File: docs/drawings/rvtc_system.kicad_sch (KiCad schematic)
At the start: 0 parts

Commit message: Diagram: add MeshCore nodes, bridge ports, other LAN hosts
From MikroTik DHCP leases: MeshCore Observer (.25, ESP32-S3, WiFi,
MQTT direct to Mosquitto) and companion (.26, RAK4631+RAK13800,
ether4, TCP to Meshy); meshcore_name_resolver.py adaptor; ether6/ether4
labels on gateway and host links; box of other RV LAN hosts (no MACs).
Title block now marks the .kicad_sch as hand-editable base layout.

Co-Authored-By: Claude Opus 5.5 <noreply@anthropic.com>
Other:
- note added: ".2 VE7CBH-RV workstation (ether4) .4 DS223 NAS (ether5) .20 printer .21 Fanvil X4G phone .22 TL-SG108PE PoE switch (ether4) .23 Motorola phone .24 WP-820 (wlan1) .254 Sonoff S31 plug (dynamic, wlan1)"
- note added: "ADVERTs -> meshcore/names/+"
- note added: "Arrow = data direction. Gateway IPs are 192.168.88.x, port 4001."
- note added: "ESP32-S3, WiFi (wlan1) MQTT meshcore/DUQ/+/* -> :1883"
- note added: "Ethernet - TCP/IP"
- note added: "MeshCore Observer .25"
- note added: "MeshCore companion .26"
- note added: "Other RV LAN hosts"
- note added: "RAK4631 + RAK13800 (WIZnet), ether4 TCP <-> Meshy app"
- note added: "Source: RVTC_System_Reference_2_15.md"
- note added: "WiFi - TCP/IP"
- note added: "ether4"
- note added: "ether6"
- note added: "meshcore/DUQ/+/*: published by"
- note added: "meshcore_name_resolver.py"
- note added: "the nodes themselves (no bridge)"
- note removed: "Arrow = data direction. Gateway IPs are 192.168.88.x, port 4001. Source: RVTC_System_Reference_2_15.md"
- note removed: "Eth"

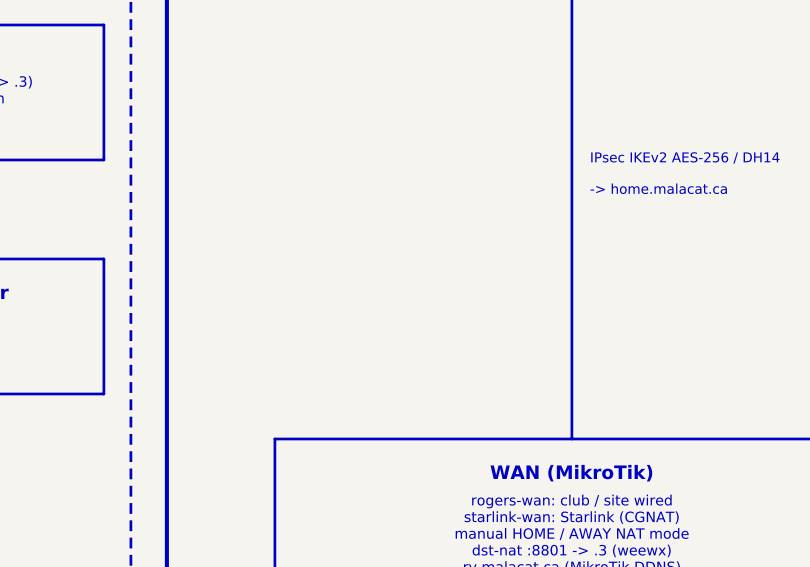
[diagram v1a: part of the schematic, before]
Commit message: Add electrical block diagram as page 2 of rvtc_system KiCad project
New rvtc_power.kicad_sch (+ generator): PV -> MPPT60 -> LiFePO4 bank
(main fuse, 300 A shunt, single-point ground) -> 12 V DC bus feeding the
OEM DC load centre, RVTC 12 V kit and the EVO-2212; shore/gen inlets with
KWS meters -> transfer -> EVO -> AC load centre, load-shed relays, A/C,
heater plugs, J45 monitors/speakers (the only AC-powered RVTC items).
Undocumented values marked "?" for hand completion.

rvtc_system.kicad_sch gets an "Electrical" sheet symbol linking page 2;
minimal rvtc_system.kicad_pro added so both open as one project.

Co-Authored-By: Claude Opus 5.5 <noreply@anthropic.com>
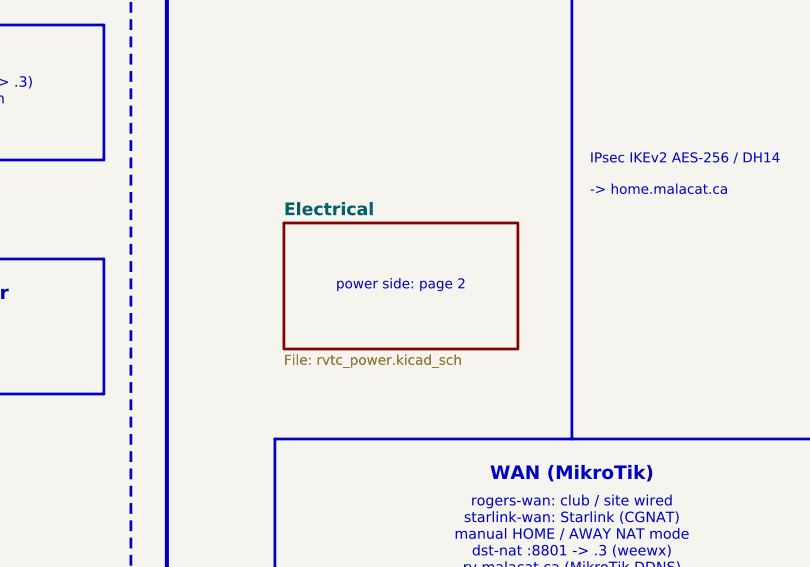
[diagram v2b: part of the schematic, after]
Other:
- added sheet Electrical (rvtc_power.kicad_sch)
- note added: "power side: page 2"
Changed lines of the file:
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@@
     (company "RVTC - VE7CBH")
     (comment 1 "Block-diagram style - not a manufacturable schematic")
-    (comment 2 "Base layout from docs/drawings/generate_rvtc_system_sch.py - hand-edited since; re-running it overwrites edits")
+    (comment 2 "Base layout: generate_rvtc_system_sch.py; hand-edited after - re-running overwrites")
   )
   (text "RV Total Control (RVTC) - System Block Diagram" (exclude_from_sim no) (at 12 14 0)
@@
     (effects (font (size 1.0 1.0)) (justify left))
   )
+  (sheet (at 343 172) (size 26 14) (fields_autoplaced yes)
+    (stroke (width 0.3) (type solid) (color 180 0 0 1))
+    (fill (color 253 230 230 1))
+    (property "Sheetname" "Electrical" (at 343 171.3 0)
+      (effects (font (size 1.4 1.4) bold) (justify left bottom))
+    )
+    (property "Sheetfile" "rvtc_power.kicad_sch" (at 343 186.6 0)
+      (effects (font (size 1.1 1.1)) (justify left top))
+    )
+    (instances
+      (project "rvtc_system"
+        (path "/7bcc9a8a-ae26-44fa-87de-cee0a644d8cb" (page "2"))
+      )
+    )
+  )
+  (text "power side: page 2" (exclude_from_sim no) (at 356 179 0)
+    (effects (font (size 1.1 1.1)))
+  )
   (sheet_instances

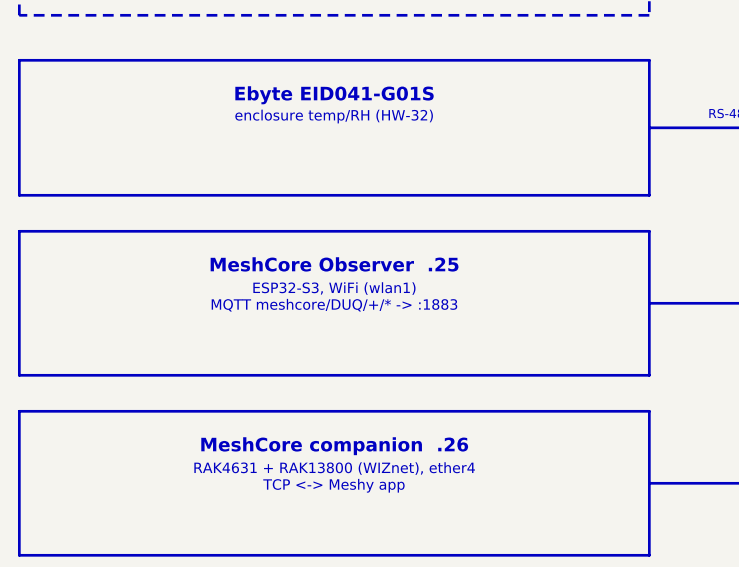
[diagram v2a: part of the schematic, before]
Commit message: Drawings: observer is a LilyGo T-Beam; fill in PV array from datasheet
Page 1: MeshCore Observer box now names VE7CBH-RVTC (LilyGo T-Beam,
DUQ, also reports to the public observer map) instead of "ESP32-S3".

Page 2 (includes the owner's hand edits so far, e.g. DC load centre
fuse 70 A and 3 string lines): PV array is 9 x Renogy RNG-100D-SS,
3S3P = 900 W; array Voc 72.9 V / Isc 15.6 A, Vmp 61.2 V / Imp 14.7 A
(from the panel datasheet). Combiner notes the 15 A panel max series
fuse rating.

Co-Authored-By: Claude Opus 5.5 <noreply@anthropic.com>
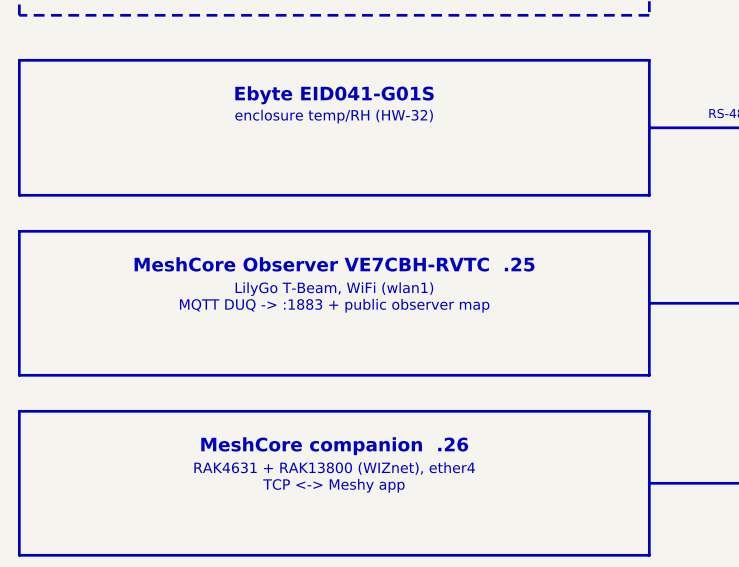
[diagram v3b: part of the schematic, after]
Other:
- note added: "LilyGo T-Beam, WiFi (wlan1) MQTT DUQ -> :1883 + public observer map"
- note added: "MeshCore Observer VE7CBH-RVTC .25"
- note removed: "ESP32-S3, WiFi (wlan1) MQTT meshcore/DUQ/+/* -> :1883"
- note removed: "MeshCore Observer .25"
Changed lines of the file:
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@@
     (fill (type color) (color 225 236 252 1))
   )
-  (text "MeshCore Observer  .25" (exclude_from_sim no) (at 47.0 253 0)
+  (text "MeshCore Observer VE7CBH-RVTC  .25" (exclude_from_sim no) (at 47.0 253 0)
     (effects (font (size 1.5 1.5) bold (color 0 70 160 1)))
   )
-  (text "ESP32-S3, WiFi (wlan1)\nMQTT meshcore/DUQ/+/* -> :1883" (exclude_from_sim no) (at 47.0 256.5 0)
+  (text "LilyGo T-Beam, WiFi (wlan1)\nMQTT DUQ -> :1883 + public observer map" (exclude_from_sim no) (at 47.0 256.5 0)
     (effects (font (size 1.15 1.15)))
   )

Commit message: Drawings: 11x17, single Waveshare 8-port unit, two DC distributions
- Both sheets now USLedger (11x17); layouts compressed vertically to fit.
- Page 1: the eight 485-x gateways are one Waveshare 8-port RS-485/ETH
  unit (one IP per port), drawn as a single box like the HF5142B.
- Page 2: filled from the parts list (items carried over from the Cougar
  build): 350 A ANL main fuse + Ampper switch, ECO-WORTHY combiner (12 A
  per string), BlueFire fuse box, 30 A shore/gen cords + DIN breakers,
  WFCO OEM load centre, EVO-RC+ remote, Sony/Sceptre monitors. Flags the
  80 V-rated Americal DIN breaker vs ~86 V cold array Voc.
- Two DC distribution points: forward electrical bay bus bars and the
  WFCO OEM load centre, fed through a 250 A main DC fuse.
- Page 1 generator emits 11x17 directly.

Co-Authored-By: Claude Opus 5.5 <noreply@anthropic.com>
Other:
- note added: "485-1 192.168.88.5:4001"
- note added: "485-2 192.168.88.6:4001"
- note added: "485-3 192.168.88.7:4001"
- note added: "485-4 192.168.88.8:4001"
- note added: "485-5 192.168.88.9:4001"
- note added: "485-6 192.168.88.10:4001"
- note added: "485-7 192.168.88.11:4001"
- note added: "485-8 192.168.88.12:4001"
- note added: "RS-485 to Ethernet, Protocol: None"
- note added: "Waveshare 8-port"
- note removed: "192.168.88.10:4001 Protocol: None"
- note removed: "192.168.88.11:4001 Protocol: None"
- note removed: "192.168.88.12:4001 Protocol: None"
- note removed: "192.168.88.5:4001 Protocol: None"
- note removed: "192.168.88.6:4001 Protocol: None"
- note removed: "192.168.88.7:4001 Protocol: None"
- note removed: "192.168.88.8:4001 Protocol: None"
- note removed: "192.168.88.9:4001 Protocol: None"
- note removed: "485-1 Waveshare"
- note removed: "485-2 Waveshare"
- note removed: "485-3 Waveshare"
- note removed: "485-4 Waveshare"
- note removed: "485-5 Waveshare"
- note removed: "485-6 Waveshare"
- note removed: "485-7 Waveshare"
- note removed: "485-8 Waveshare"
